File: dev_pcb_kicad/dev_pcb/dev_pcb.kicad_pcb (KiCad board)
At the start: 2 copper layers, 33 x 37.5 mm, 11 parts, among them U2 XIAO-ESP32-S3-DIP

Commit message: .
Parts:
- moved R2 0.50 mm to (70.5, 87.0)
- moved R3 0.50 mm to (70.5, 83.0)
- moved R4 0.50 mm to (70.5, 79.0)
- moved R5 0.50 mm to (70.5, 75.0)
- renumbered D3 to RX, D1 to RXOK, D2 to SFD, D4 to TX
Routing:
- net +3.3V: track 87.7 -> 61.0 mm
- net GND: track 8.29 -> 6.58 mm, vias 6 -> 16
- net Net-(DWM1-IRQ/GPIO8): track 23.2 -> 21.6 mm
- net Net-(DWM1-SPIMISO): track 32.5 -> 33.9 mm
- net Net-(DWM1-SPICLK): track 44.9 -> 43.6 mm
- net Net-(DWM1-SPIMOSI): track 32.3 -> 31.3 mm
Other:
- board size 33 x 37.5 mm -> 29.5 x 38.5 mm

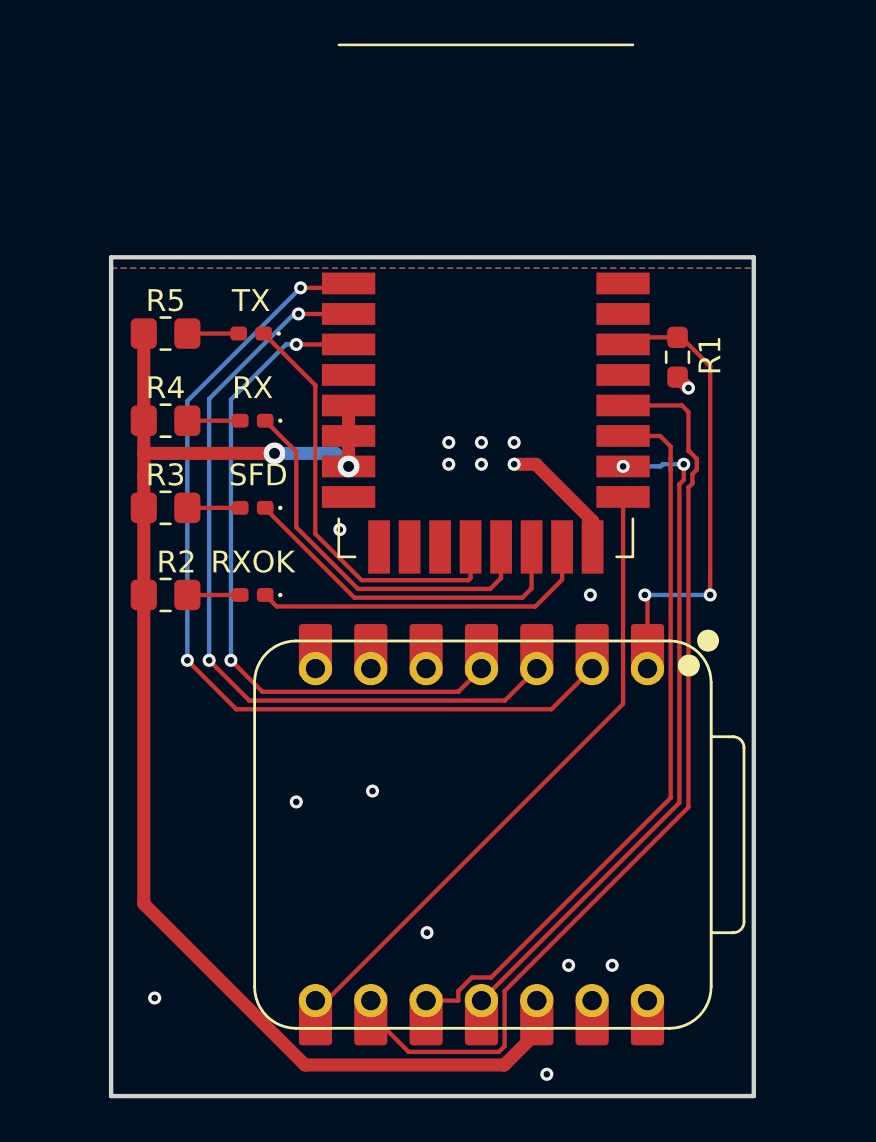
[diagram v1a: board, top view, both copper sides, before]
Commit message: small tracing fixes
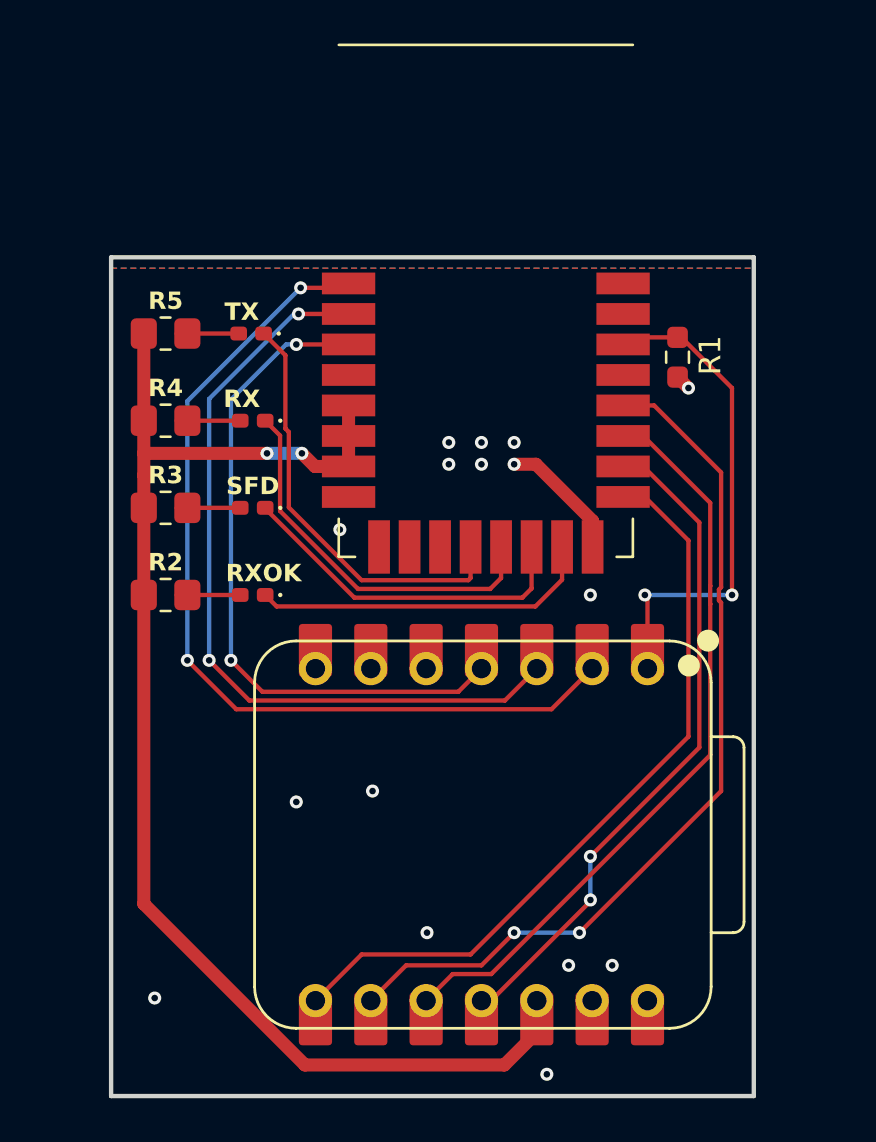
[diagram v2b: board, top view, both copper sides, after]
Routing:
- net Net-(DWM1-~{SPICS}): track 29.8 -> 35.3 mm
- net Net-(DWM1-SPICLK): track 43.6 -> 41.2 mm, vias 0 -> 2
- net Net-(DWM1-IRQ/GPIO8): track 21.6 -> 23.0 mm
- net Net-(DWM1-SPIMISO): track 33.9 -> 34.6 mm

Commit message: probe points
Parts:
- added CLK: MISO, TestPoint:TestPoint_Pad_D1.0mm, F.Cu at (99.0, 80.5)
- added EXTON: TestPoint_Probe, TestPoint:TestPoint_Pad_D1.0mm, F.Cu at (99.0, 104.5)
- added IRQ: TestPoint_Probe, TestPoint:TestPoint_Pad_D1.0mm, F.Cu at (99.0, 99.0)
- added MISO: CLK, TestPoint:TestPoint_Pad_D1.0mm, F.Cu at (99.0, 84.5)
- added MOSI: MOSI, TestPoint:TestPoint_Pad_D1.0mm, F.Cu at (99.0, 76.5)
- added WAKEUP: TestPoint_Probe, TestPoint:TestPoint_Pad_D1.0mm, F.Cu at (99.0, 93.5)
- renumbered RX to RX1, RXOK to RXOK1, SFD to SFD1, TX to TX1
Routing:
- net Net-(DWM1-EXTON): track 41.7 -> 58.5 mm, vias 2 -> 4
- net Net-(DWM1-WAKEUP): track 36.4 -> 49.9 mm, vias 2 -> 4
- net Net-(DWM1-IRQ/GPIO8): track 23.0 -> 34.3 mm, vias 2 -> 4
- net Net-(DWM1-SPIMOSI): track 30.9 -> 38.8 mm, vias 2 -> 4
- net Net-(DWM1-SPIMISO): track 34.6 -> 40.3 mm, vias 0 -> 2
- net Net-(DWM1-SPICLK): track 41.2 -> 44.8 mm, vias 2 -> 4
- net GND: track 6.58 -> 7.29 mm, vias 16 -> 18
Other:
- board size 29.5 x 38.5 mm -> 33 x 38.5 mm
